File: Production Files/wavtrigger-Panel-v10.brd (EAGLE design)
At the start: 147.8 x 139.7 mm, 439 parts, among them J1 5.5x2.1mm Barrel, J10 5.5x2.1mm Barrel, J12 USD-SOCKETNEW, J15 M08X2, J17 M08X2, J19 5.5x2.1mm Barrel, J21 USD-SOCKETNEW, J24 M08X2, J26 M08X2, J28 5.5x2.1mm Barrel, J3 USD-SOCKETNEW, J30 USD-SOCKETNEW, J33 M08X2, J35 M08X2, J6 M08X2, J7 M08X2, U11 STM32F405RG, U12 MIC5323-3.3, U13 PCM5100, U14 LM4990, U16 STM32F405RG, U17 MIC5323-3.3, U18 PCM5100, U19 LM4990, U2 MIC5323-3.3, U3 STM32F405RG, U4 STM32F405RG, U5 PCM5100, U6 LM4990, U7 MIC5323-3.3, U8 PCM5100, U9 LM4990, Y1 8MHz, Y2 8MHz, Y3 8MHz, Y4 8MHz

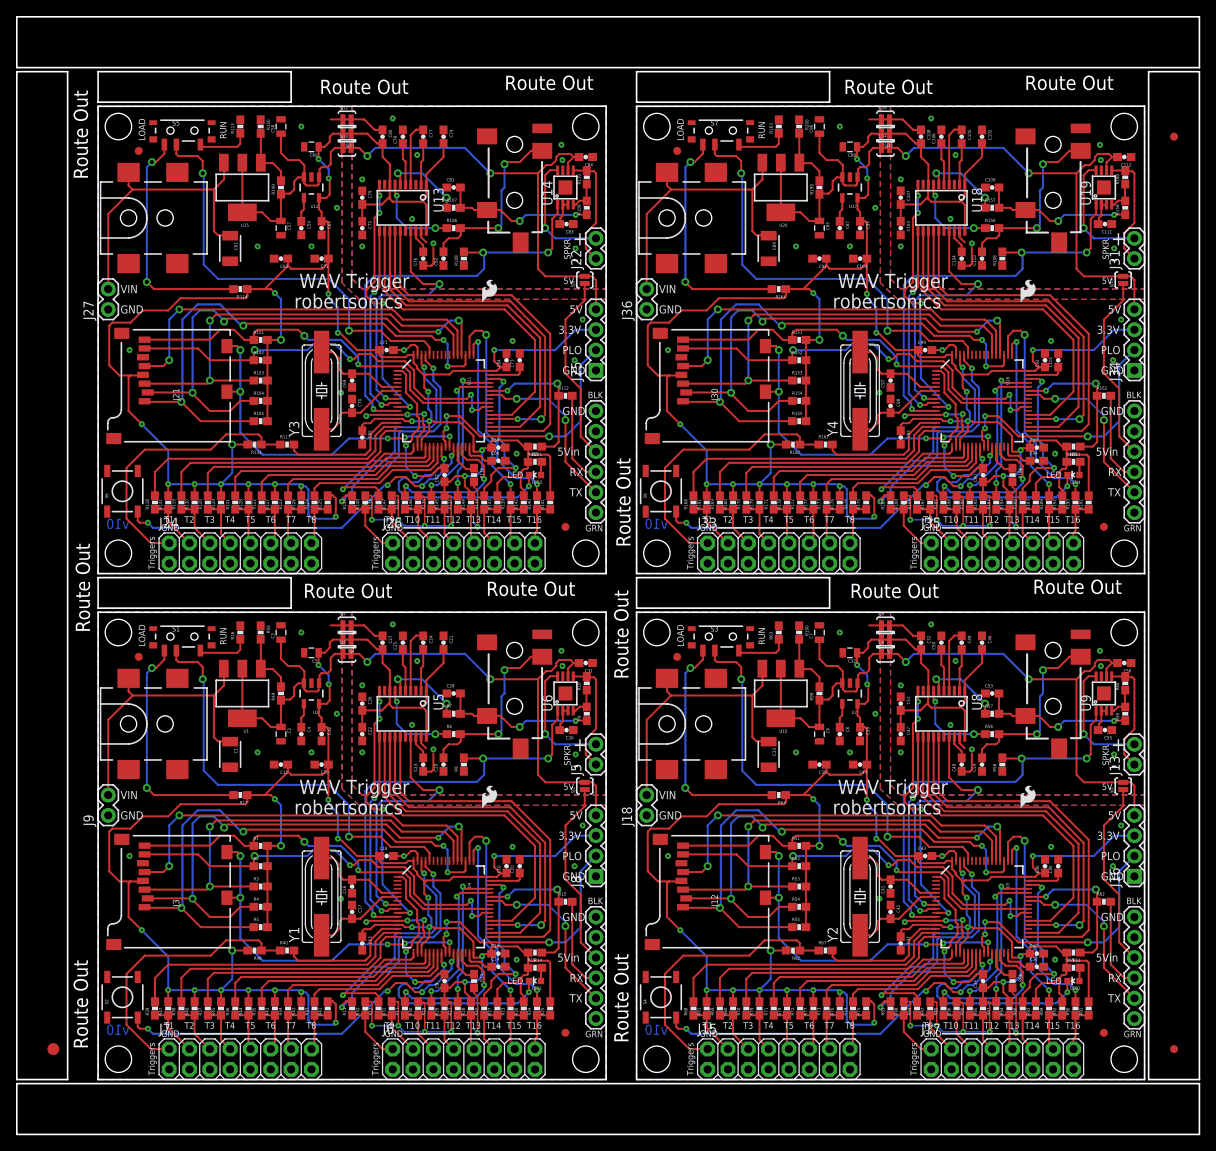
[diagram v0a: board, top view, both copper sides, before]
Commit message: Reverting back to panel v10
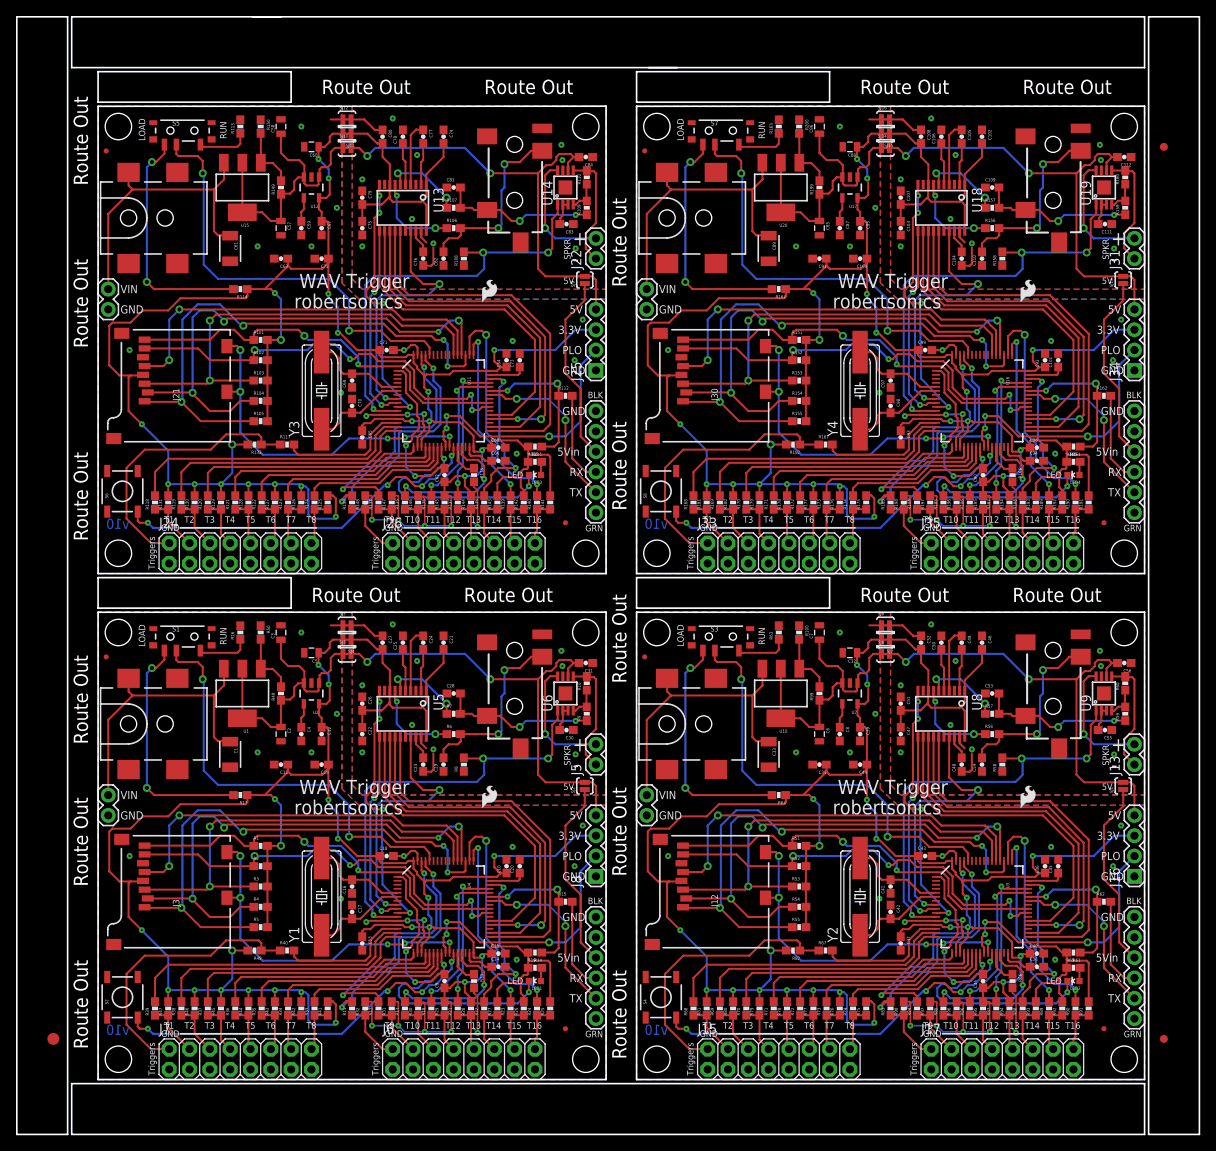
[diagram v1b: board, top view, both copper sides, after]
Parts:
- removed E$6: (no value), SparkFun-Aesthetics:FIDUCIAL-1X2
- added E$4: (no value), SparkFun-Aesthetics:FIDUCIAL-1X2
- C105, C106, C24, C25, C49, C50, C77, C78: value 2.2uF -> 0.1uF
- E$1: device SparkFun-Retired:FIDUCIAL-1.5X3 -> SparkFun-Aesthetics:FIDUCIAL-1.5X3
- FID1, FID2, FID3, FID4, FID5, FID6, FID7, FID8: value FIDUCIAL1X2 -> FIDUCIALUFIDUCIAL; device SparkFun-Aesthetics:FIDUCIAL-1X2 -> SparkFun-Aesthetics:MICRO-FIDUCIAL
- moved E$5 112.8 mm to (143.4, 123.4), turned to 180 degrees
- moved FID1 4.06 mm to (11.2, 59.7)
- moved FID5 4.06 mm to (11.2, 122.9)
- moved FID3 4.06 mm to (78.5, 59.7)
- moved FID7 4.06 mm to (78.5, 122.9)
- moved E$1 1.27 mm to (4.57, 11.9)
- moved FID2 0.51 mm to (68.6, 13.2)
- moved FID4 0.51 mm to (135.9, 13.2)
- moved FID6 0.51 mm to (68.6, 76.5)
- moved FID8 0.51 mm to (135.9, 76.5)
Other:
- outline, holes or cut-outs redrawn
